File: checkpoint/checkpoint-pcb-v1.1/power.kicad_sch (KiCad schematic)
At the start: 21 parts, among them J17 PWR_CAN_IN, J18 PWR_OUT, U5 AMS1117-3.3, U6 TPS5430DDA

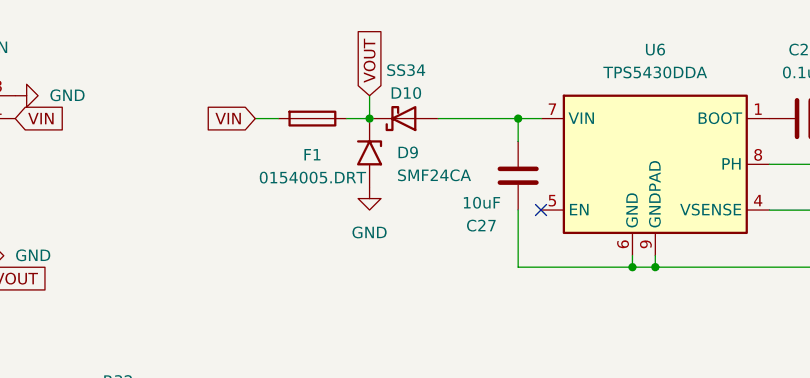
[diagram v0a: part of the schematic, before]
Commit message: fix: rotate backwards filter diode
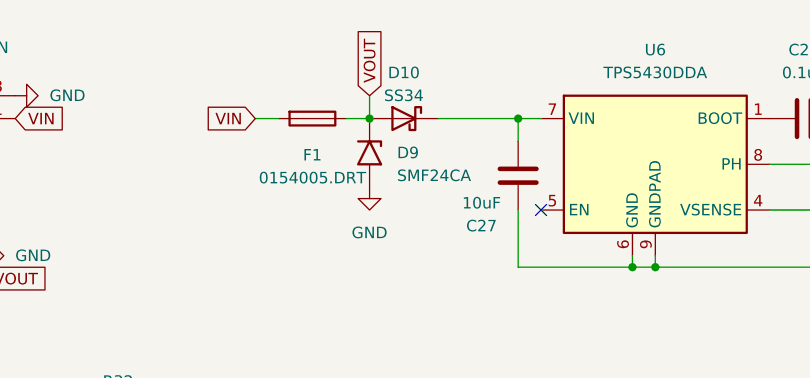
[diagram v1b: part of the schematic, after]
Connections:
- net VOUT: now also D10.2 (A); no longer D10.1 (K)
- net at C27.1, U6.7 (VIN): now also D10.1 (K); no longer D10.2 (A)
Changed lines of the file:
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@@
 		(lib_id "Diode:SS34")
 		(at 99.06 77.47 0)
-		(mirror x)
+		(mirror y)
 		(unit 1)
 		(exclude_from_sim no)
@@
 		(dnp no)
 		(property "Reference" "D10"
-			(at 99.314 74.676 0)
+			(at 99.06 72.39 0)
 			(effects
 				(font
@@
 		)
 		(property "Value" "SS34"
-			(at 99.314 72.136 0)
+			(at 99.06 74.93 0)
 			(effects
 				(font
@@
 		)
 		(property "Footprint" "Diode_SMD:D_SMA"
-			(at 99.06 73.025 0)
+			(at 99.06 81.915 0)
 			(effects
 				(font

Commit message: chore: reset refdes numbers
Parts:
- renumbered J17 to J19
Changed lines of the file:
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@@
 		(dnp no)
 		(fields_autoplaced yes)
-		(property "Reference" "#PWR052"
+		(property "Reference" "#PWR054"
 			(at 38.1 113.03 0)
 			(effects
@@
 			(project "checkpoint"
 				(path "/3a22685f-fb6f-4c54-b509-09f3e7d2168e/802d63ea-9e17-41b2-878e-1c963e32b520"
-					(reference "#PWR052")
+					(reference "#PWR054")
 					(unit 1)
 				)
@@
 		(dnp no)
 		(fields_autoplaced yes)
-		(property "Reference" "#PWR059"
+		(property "Reference" "#PWR061"
 			(at 179.07 100.33 0)
 			(effects
@@
 			(project "checkpoint"
 				(path "/3a22685f-fb6f-4c54-b509-09f3e7d2168e/802d63ea-9e17-41b2-878e-1c963e32b520"
-					(reference "#PWR059")
+					(reference "#PWR061")
 					(unit 1)
 				)
@@
 		(dnp no)
 		(fields_autoplaced yes)
-		(property "Reference" "#PWR053"
+		(property "Reference" "#PWR055"
 			(at 41.91 127 0)
 			(effects
@@
 			(project "checkpoint"
 				(path "/3a22685f-fb6f-4c54-b509-09f3e7d2168e/802d63ea-9e17-41b2-878e-1c963e32b520"
-					(reference "#PWR053")
+					(reference "#PWR055")
 					(unit 1)
 				)
@@
 		(dnp no)
 		(fields_autoplaced yes)
-		(property "Reference" "#PWR057"
+		(property "Reference" "#PWR059"
 			(at 95.25 91.44 0)
 			(effects
@@
 			(project "checkpoint"
 				(path "/3a22685f-fb6f-4c54-b509-09f3e7d2168e/802d63ea-9e17-41b2-878e-1c963e32b520"
-					(reference "#PWR057")
+					(reference "#PWR059")
 					(unit 1)
 				)
@@
 		(dnp no)
 		(fields_autoplaced yes)
-		(property "Reference" "#PWR058"
+		(property "Reference" "#PWR060"
 			(at 179.07 81.28 0)
 			(effects
@@
 			(project "checkpoint"
 				(path "/3a22685f-fb6f-4c54-b509-09f3e7d2168e/802d63ea-9e17-41b2-878e-1c963e32b520"
-					(reference "#PWR058")
+					(reference "#PWR060")
 					(unit 1)
 				)
@@
 		(dnp no)
 		(fields_autoplaced yes)
-		(property "Reference" "#PWR054"
+		(property "Reference" "#PWR058"
 			(at 60.96 116.84 0)
 			(effects
@@
 			(project "checkpoint"
 				(path "/3a22685f-fb6f-4c54-b509-09f3e7d2168e/802d63ea-9e17-41b2-878e-1c963e32b520"
-					(reference "#PWR054")
+					(reference "#PWR058")
 					(unit 1)
 				)
@@
 		(dnp no)
 		(fields_autoplaced yes)
-		(property "Reference" "#PWR055"
+		(property "Reference" "#PWR057"
 			(at 62.23 74.93 0)
 			(effects
@@
 			(project "checkpoint"
 				(path "/3a22685f-fb6f-4c54-b509-09f3e7d2168e/802d63ea-9e17-41b2-878e-1c963e32b520"
-					(reference "#PWR055")
+					(reference "#PWR057")
 					(unit 1)
 				)
@@
 		(on_board yes)
 		(dnp no)
-		(property "Reference" "J17"
+		(property "Reference" "J19"
 			(at 49.53 72.136 0)
 			(effects
@@
 			(project "checkpoint"
 				(path "/3a22685f-fb6f-4c54-b509-09f3e7d2168e/802d63ea-9e17-41b2-878e-1c963e32b520"
-					(reference "J17")
+					(reference "J19")
 					(unit 1)
 				)

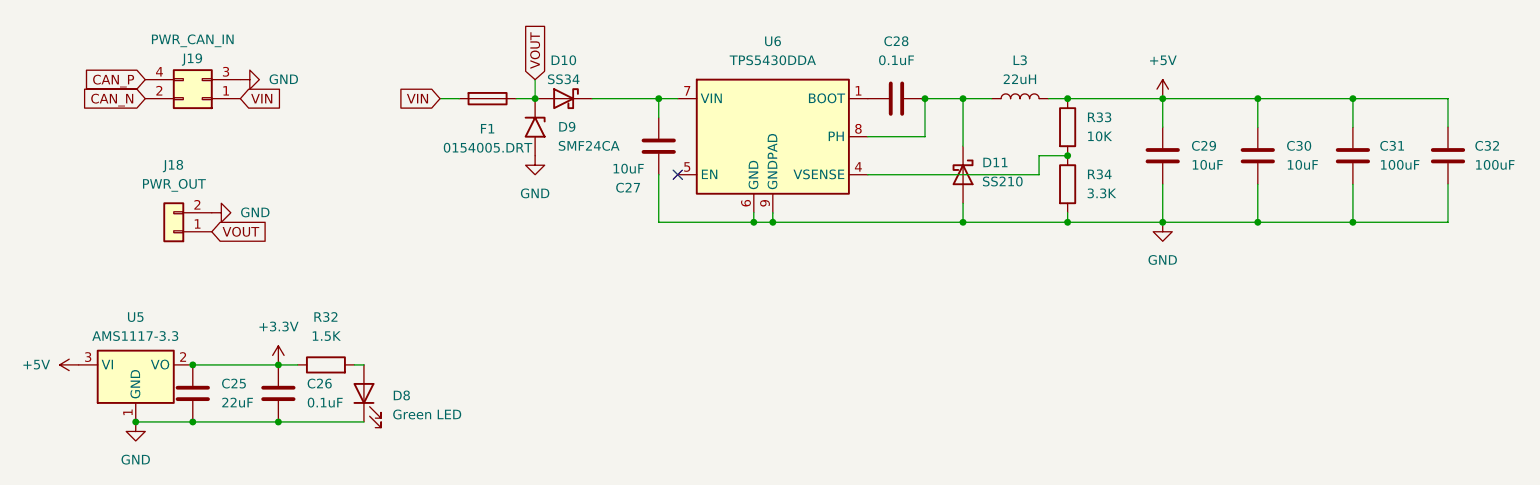
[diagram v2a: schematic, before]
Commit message: fix: add i2c pullup resistors
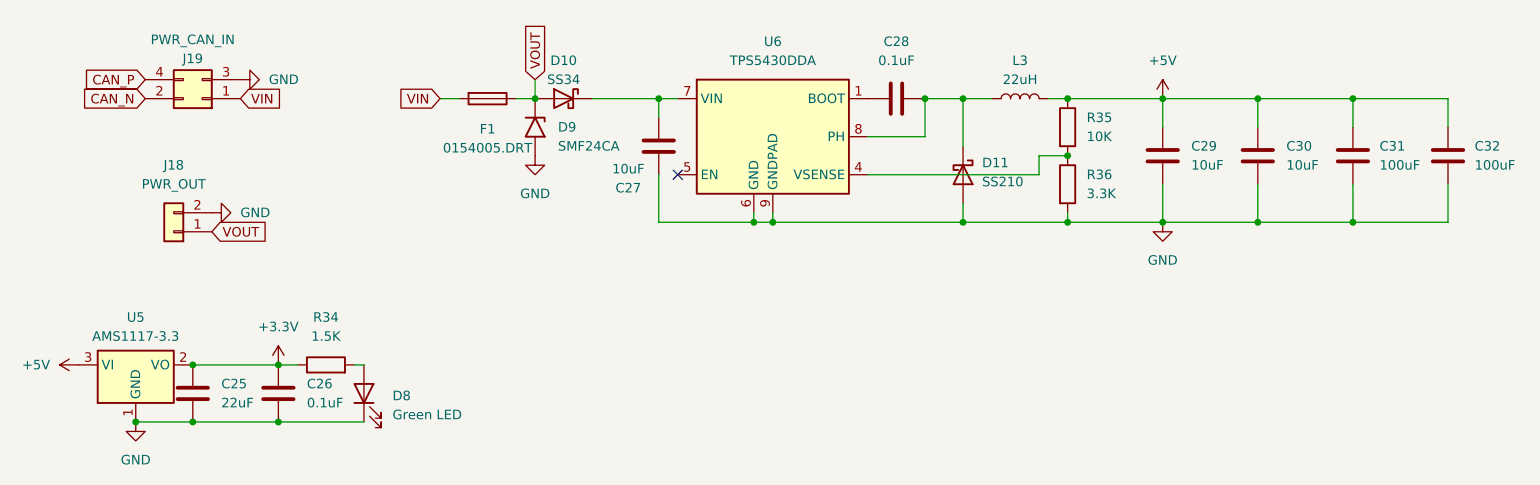
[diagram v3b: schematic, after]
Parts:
- renumbered R32 to R34, R33 to R35, R34 to R36
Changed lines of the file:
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@@
 		(dnp no)
 		(fields_autoplaced yes)
-		(property "Reference" "R32"
+		(property "Reference" "R34"
 			(at 67.31 106.68 90)
 			(effects
@@
 			(project "checkpoint"
 				(path "/3a22685f-fb6f-4c54-b509-09f3e7d2168e/802d63ea-9e17-41b2-878e-1c963e32b520"
-					(reference "R32")
+					(reference "R34")
 					(unit 1)
 				)
@@
 		(dnp no)
 		(fields_autoplaced yes)
-		(property "Reference" "R34"
+		(property "Reference" "R36"
 			(at 168.91 87.6299 0)
 			(effects
@@
 			(project "checkpoint"
 				(path "/3a22685f-fb6f-4c54-b509-09f3e7d2168e/802d63ea-9e17-41b2-878e-1c963e32b520"
-					(reference "R34")
+					(reference "R36")
 					(unit 1)
 				)
@@
 		(dnp no)
 		(fields_autoplaced yes)
-		(property "Reference" "#PWR054"
+		(property "Reference" "#PWR055"
 			(at 38.1 113.03 0)
 			(effects
@@
 			(project "checkpoint"
 				(path "/3a22685f-fb6f-4c54-b509-09f3e7d2168e/802d63ea-9e17-41b2-878e-1c963e32b520"
-					(reference "#PWR054")
+					(reference "#PWR055")
 					(unit 1)
 				)
@@
 		(dnp no)
 		(fields_autoplaced yes)
-		(property "Reference" "#PWR061"
+		(property "Reference" "#PWR062"
 			(at 179.07 100.33 0)
 			(effects
@@
 			(project "checkpoint"
 				(path "/3a22685f-fb6f-4c54-b509-09f3e7d2168e/802d63ea-9e17-41b2-878e-1c963e32b520"
-					(reference "#PWR061")
+					(reference "#PWR062")
 					(unit 1)
 				)
@@
 		(dnp no)
 		(fields_autoplaced yes)
-		(property "Reference" "#PWR056"
+		(property "Reference" "#PWR057"
 			(at 58.42 92.71 0)
 			(effects
@@
 			(project "checkpoint"
 				(path "/3a22685f-fb6f-4c54-b509-09f3e7d2168e/802d63ea-9e17-41b2-878e-1c963e32b520"
-					(reference "#PWR056")
+					(reference "#PWR057")
 					(unit 1)
 				)
@@
 		(dnp no)
 		(fields_autoplaced yes)
-		(property "Reference" "#PWR055"
+		(property "Reference" "#PWR056"
 			(at 41.91 127 0)
 			(effects
@@
 			(project "checkpoint"
 				(path "/3a22685f-fb6f-4c54-b509-09f3e7d2168e/802d63ea-9e17-41b2-878e-1c963e32b520"
-					(reference "#PWR055")
+					(reference "#PWR056")
 					(unit 1)
 				)
@@
 		(dnp no)
 		(fields_autoplaced yes)
-		(property "Reference" "#PWR059"
+		(property "Reference" "#PWR060"
 			(at 95.25 91.44 0)
 			(effects
@@
 			(project "checkpoint"
 				(path "/3a22685f-fb6f-4c54-b509-09f3e7d2168e/802d63ea-9e17-41b2-878e-1c963e32b520"
-					(reference "#PWR059")
+					(reference "#PWR060")
 					(unit 1)
 				)
@@
 		(dnp no)
 		(fields_autoplaced yes)
-		(property "Reference" "R33"
+		(property "Reference" "R35"
 			(at 168.91 80.0099 0)
 			(effects
@@
 			(project "checkpoint"
 				(path "/3a22685f-fb6f-4c54-b509-09f3e7d2168e/802d63ea-9e17-41b2-878e-1c963e32b520"
-					(reference "R33")
+					(reference "R35")
 					(unit 1)
 				)
@@
 		(dnp no)
 		(fields_autoplaced yes)
-		(property "Reference" "#PWR060"
+		(property "Reference" "#PWR061"
 			(at 179.07 81.28 0)
 			(effects
@@
 			(project "checkpoint"
 				(path "/3a22685f-fb6f-4c54-b509-09f3e7d2168e/802d63ea-9e17-41b2-878e-1c963e32b520"
-					(reference "#PWR060")
+					(reference "#PWR061")
 					(unit 1)
 				)
@@
 		(dnp no)
 		(fields_autoplaced yes)
-		(property "Reference" "#PWR058"
+		(property "Reference" "#PWR059"
 			(at 60.96 116.84 0)
 			(effects
@@
 			(project "checkpoint"
 				(path "/3a22685f-fb6f-4c54-b509-09f3e7d2168e/802d63ea-9e17-41b2-878e-1c963e32b520"
-					(reference "#PWR058")
+					(reference "#PWR059")
 					(unit 1)
 				)
@@
 		(dnp no)
 		(fields_autoplaced yes)
-		(property "Reference" "#PWR057"
+		(property "Reference" "#PWR058"
 			(at 62.23 74.93 0)
 			(effects
@@
 			(project "checkpoint"
 				(path "/3a22685f-fb6f-4c54-b509-09f3e7d2168e/802d63ea-9e17-41b2-878e-1c963e32b520"
-					(reference "#PWR057")
+					(reference "#PWR058")
 					(unit 1)
 				)

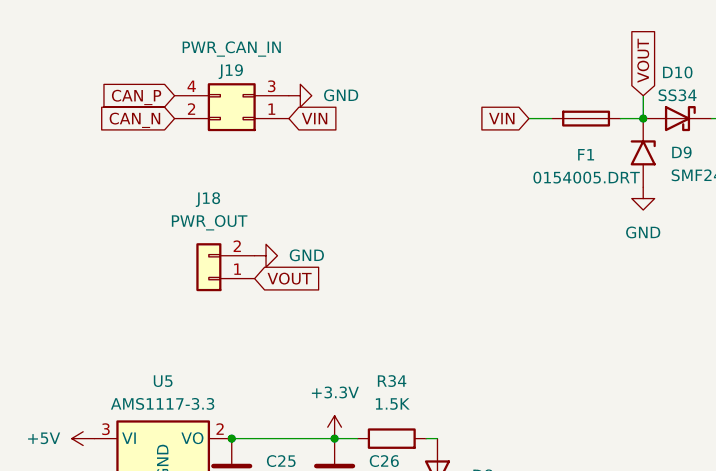
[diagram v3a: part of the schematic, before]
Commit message: fix: swap can lines to match BTT convention
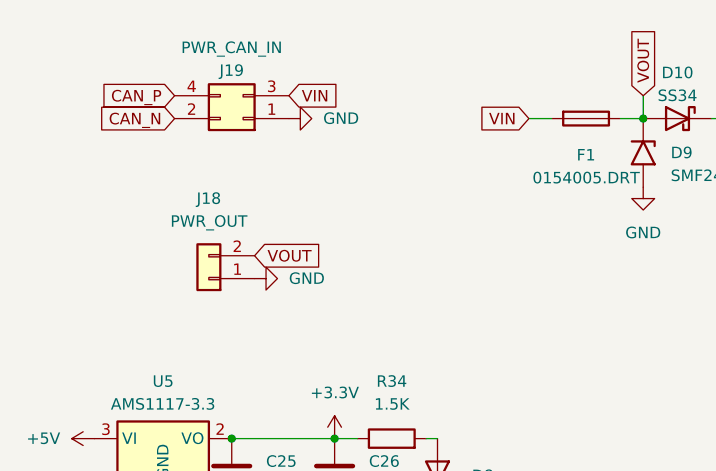
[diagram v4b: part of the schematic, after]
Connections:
- net GND: now also J18.1 (Pin_1), J19.1 (Pin_1); no longer J18.2 (Pin_2), J19.3 (Pin_3)
- net VIN: now also J19.3 (Pin_3); no longer J19.1 (Pin_1)
- net VOUT: now also J18.2 (Pin_2); no longer J18.1 (Pin_1)
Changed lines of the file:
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@@
 	(global_label "VOUT"
 		(shape input)
-		(at 52.07 95.25 0)
+		(at 52.07 92.71 0)
 		(fields_autoplaced yes)
 		(effects
@@
 		)
 		(property "Intersheetrefs" "${INTERSHEET_REFS}"
-			(at 59.7724 95.25 0)
+			(at 59.7724 92.71 0)
 			(effects
 				(font
@@
 	(global_label "VIN"
 		(shape input)
-		(at 55.88 77.47 0)
+		(at 55.88 74.93 0)
 		(fields_autoplaced yes)
 		(effects
@@
 		)
 		(property "Intersheetrefs" "${INTERSHEET_REFS}"
-			(at 61.8891 77.47 0)
+			(at 61.8891 74.93 0)
 			(effects
 				(font
@@
 	(symbol
 		(lib_id "power:GND")
-		(at 52.07 92.71 90)
+		(at 52.07 95.25 90)
 		(unit 1)
 		(exclude_from_sim no)
@@
 		(fields_autoplaced yes)
 		(property "Reference" "#PWR057"
-			(at 58.42 92.71 0)
+			(at 58.42 95.25 0)
 			(effects
 				(font
@@
 		)
 		(property "Value" "GND"
-			(at 55.88 92.7099 90)
+			(at 55.88 95.2499 90)
 			(effects
 				(font
@@
 		)
 		(property "Footprint" ""
-			(at 52.07 92.71 0)
+			(at 52.07 95.25 0)
 			(effects
 				(font
@@
 		)
 		(property "Datasheet" ""
-			(at 52.07 92.71 0)
+			(at 52.07 95.25 0)
 			(effects
 				(font
@@
 		)
 		(property "Description" "Power symbol creates a global label with name \"GND\" , ground"
-			(at 52.07 92.71 0)
+			(at 52.07 95.25 0)
 			(effects
 				(font
@@
 	(symbol
 		(lib_id "power:GND")
-		(at 55.88 74.93 90)
+		(at 55.88 77.47 90)
 		(unit 1)
 		(exclude_from_sim no)
@@
 		(fields_autoplaced yes)
 		(property "Reference" "#PWR058"
-			(at 62.23 74.93 0)
+			(at 62.23 77.47 0)
 			(effects
 				(font
@@
 		)
 		(property "Value" "GND"
-			(at 59.69 74.9299 90)
+			(at 59.69 77.4699 90)
 			(effects
 				(font
@@
 		)
 		(property "Footprint" ""
-			(at 55.88 74.93 0)
+			(at 55.88 77.47 0)
 			(effects
 				(font
@@
 		)
 		(property "Datasheet" ""
-			(at 55.88 74.93 0)
+			(at 55.88 77.47 0)
 			(effects
 				(font
@@
 		)
 		(property "Description" "Power symbol creates a global label with name \"GND\" , ground"
-			(at 55.88 74.93 0)
+			(at 55.88 77.47 0)
 			(effects
 				(font

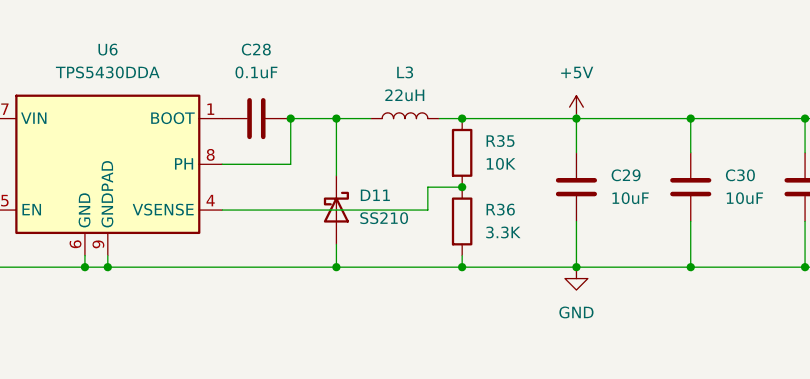
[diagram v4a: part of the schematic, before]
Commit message: feat: add inductor to support 3A@5V output
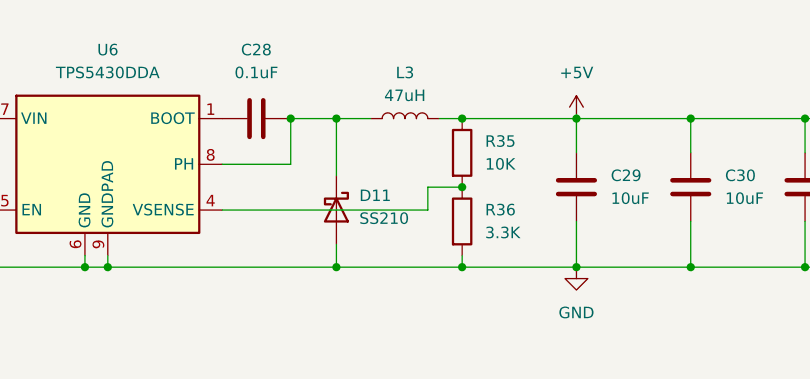
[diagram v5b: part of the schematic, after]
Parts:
- L3: value 22uH -> 47uH; footprint Library:SMMS0530 -> Library:L_Bourns_SRP7050WA_7.9x7.3mm
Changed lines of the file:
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@@
 			)
 		)
-		(property "Value" "22uH"
+		(property "Value" "47uH"
 			(at 160.02 74.93 90)
 			(effects
@@
 			)
 		)
-		(property "Footprint" "Library:SMMS0530"
+		(property "Footprint" "Library:L_Bourns_SRP7050WA_7.9x7.3mm"
 			(at 160.02 77.47 0)
 			(effects

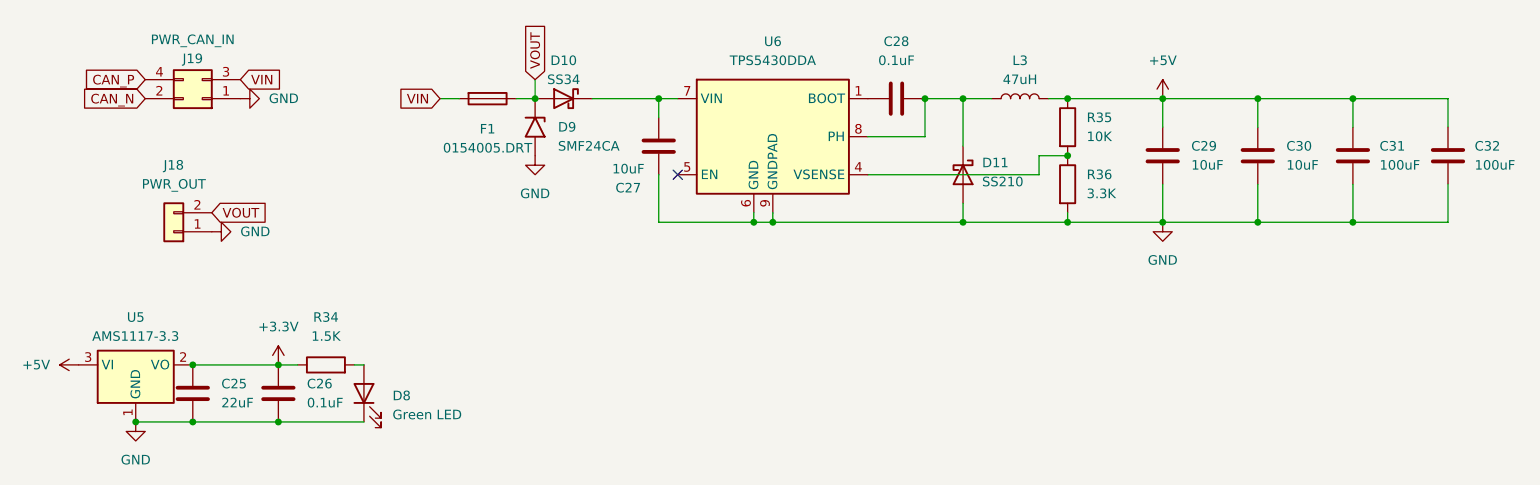
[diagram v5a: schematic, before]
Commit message: chore: update component rotation
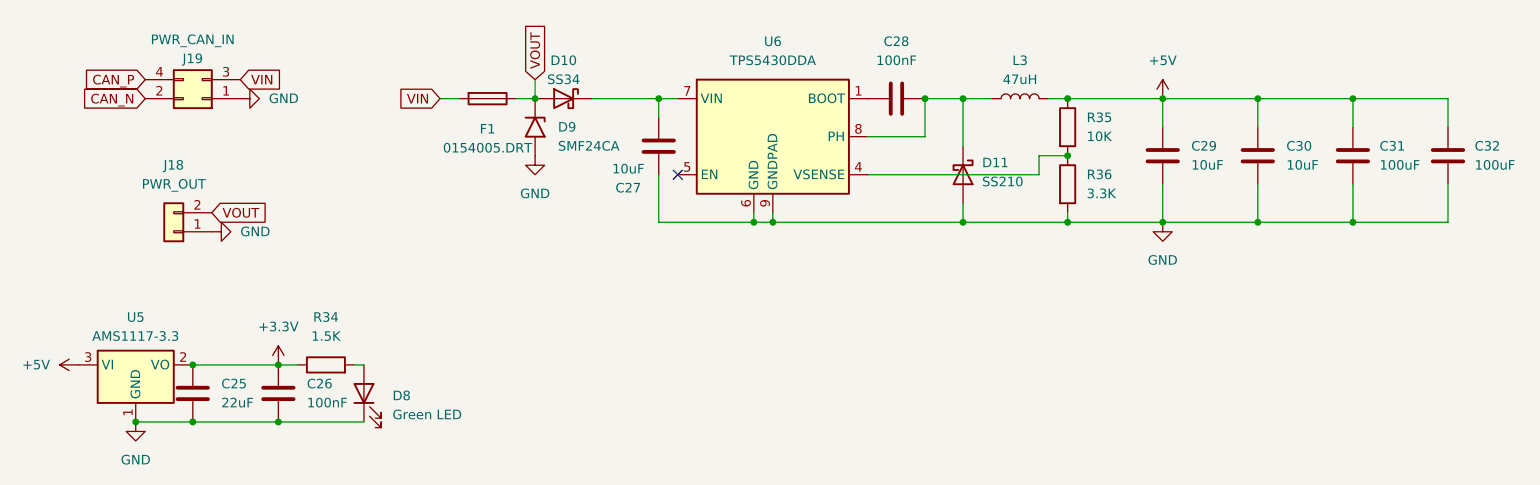
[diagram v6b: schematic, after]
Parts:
- C26, C28: value 0.1uF -> 100nF
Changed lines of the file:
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@@
 			)
 		)
-		(property "Value" "0.1uF"
+		(property "Value" "100nF"
 			(at 143.51 72.39 90)
 			(effects
@@
 			)
 		)
-		(property "Value" "0.1uF"
+		(property "Value" "100nF"
 			(at 64.77 118.1099 0)
 			(effects
